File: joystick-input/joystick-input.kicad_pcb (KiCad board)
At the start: 2 copper layers, 53.3 x 39.4 mm, 11 parts, among them J1 Conn_01x17_Male, J2 Conn_01x03_Male, J3 Conn_01x03_Male, J4 Conn_01x05_Male, J5 Conn_01x05_Male, U1 74HC165, U2 74HC165

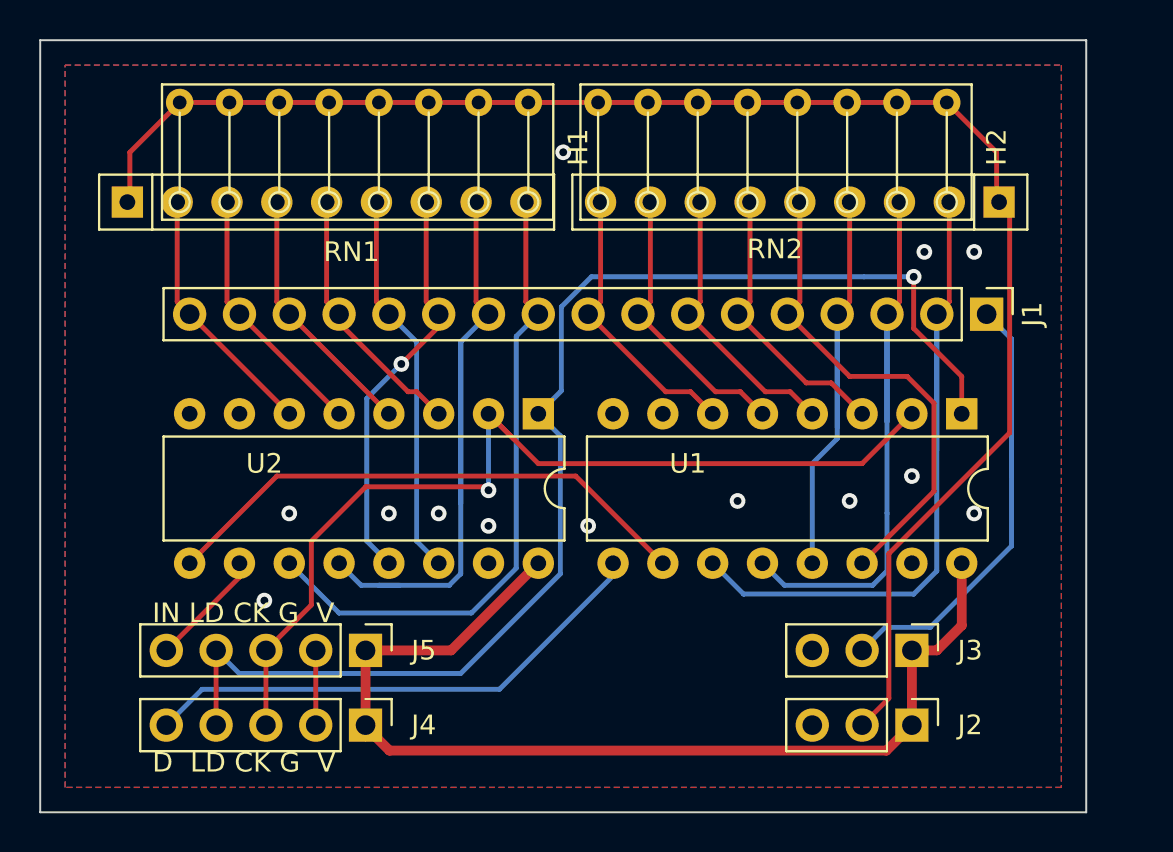
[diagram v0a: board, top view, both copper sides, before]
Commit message: joystick input 실크 텍스트 보강
Signed-off-by: Ju, Gyeong-min <jcmh74@gmail.com>
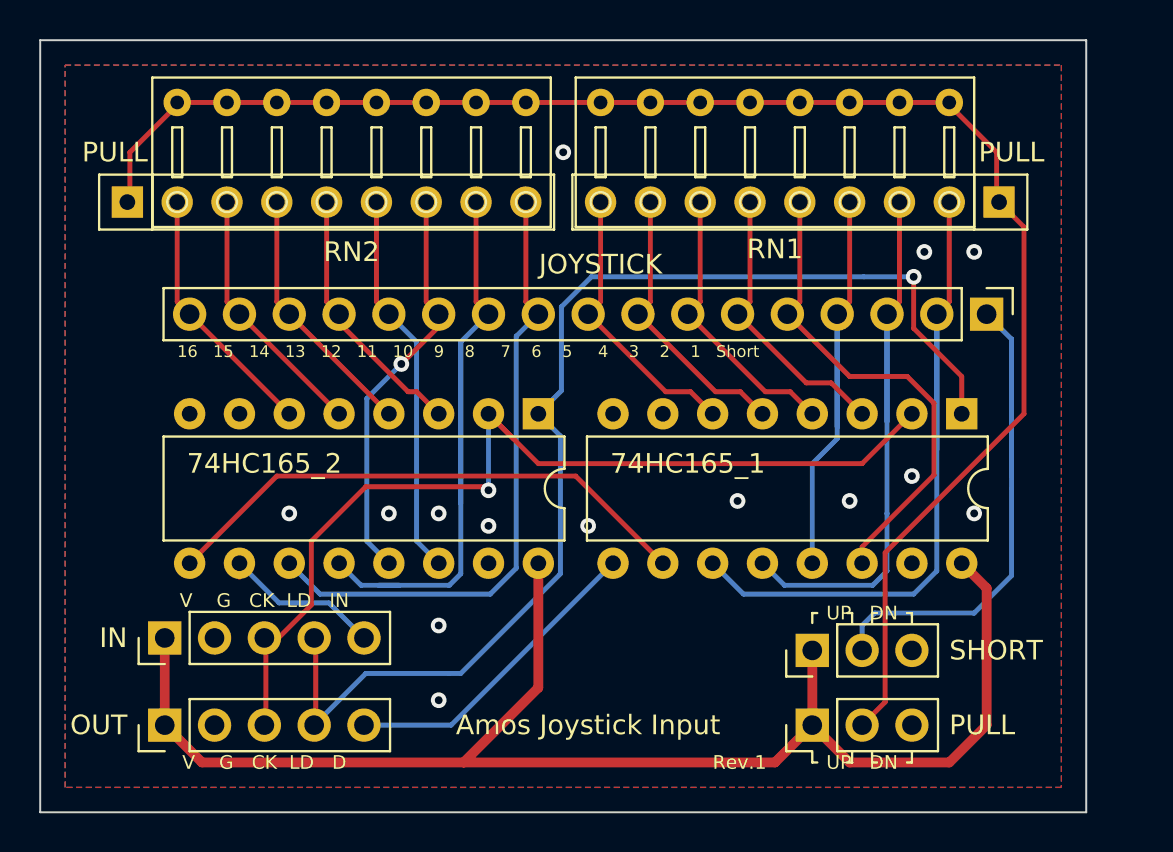
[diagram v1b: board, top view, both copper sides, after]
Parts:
- removed J4: Conn_01x05_Male, Connector_PinHeader_2.54mm:PinHeader_1x05_P2.54mm_Vertical
- added OUT: Conn_01x05_Male, Connector_PinHeader_2.54mm:PinHeader_1x05_P2.54mm_Vertical, F.Cu at (118.1, 65.4)
- moved IN 10.3 mm to (118.1, 61.0), turned to 90 degrees
- moved PULL 5.08 mm to (151.1, 65.4), turned to 90 degrees
- moved SHORT 5.08 mm to (151.1, 61.6), turned to 90 degrees
- moved H2 0.13 mm to (140.3, 38.7)
- moved H1 0.13 mm to (118.7, 38.7)
- renumbered U1 to 74HC165_1, U2 to 74HC165_2, J5 to IN, J1 to JOYSTICK, J2 to PULL, RN2 to RN1, RN1 to RN2, J3 to SHORT
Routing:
- net VCC: track 54.2 -> 73.8 mm
- net /D_OUT: track 26.6 -> 16.1 mm
- net /LOAD: track 65.1 -> 60.7 mm
- net GND: track 3.81 -> 0.00 mm, vias 13 -> 14
- net /D_IN: track 5.99 -> 8.64 mm
- net /C_SHORT: track 29.2 -> 30.8 mm
- net /C_X: track 33.0 -> 32.2 mm
- net /PULL: track 81.4 -> 82.0 mm
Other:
- board text added: "16 15 14 13 12 11 10 9 8 7 6 5 4 3 2 1 Short"
- board text added: "Amos Joystick Input"
- board text added: "PULL"
- board text added: "Rev.1"
- board text added: "UP DN"
- board text added: "V G CK LD D"
- board text added: "V G CK LD IN"
- board text removed: "D LD CK G V"
- board text removed: "IN LD CK G V"
